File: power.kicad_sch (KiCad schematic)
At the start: 28 parts, among them J3 Conn_01x02, Q2 AO3401A, SW8 SW_Slide_DPDT, U3 TP4056-42-ESOP8, U4 INA219AxDCN, U7 TPS62160DGK

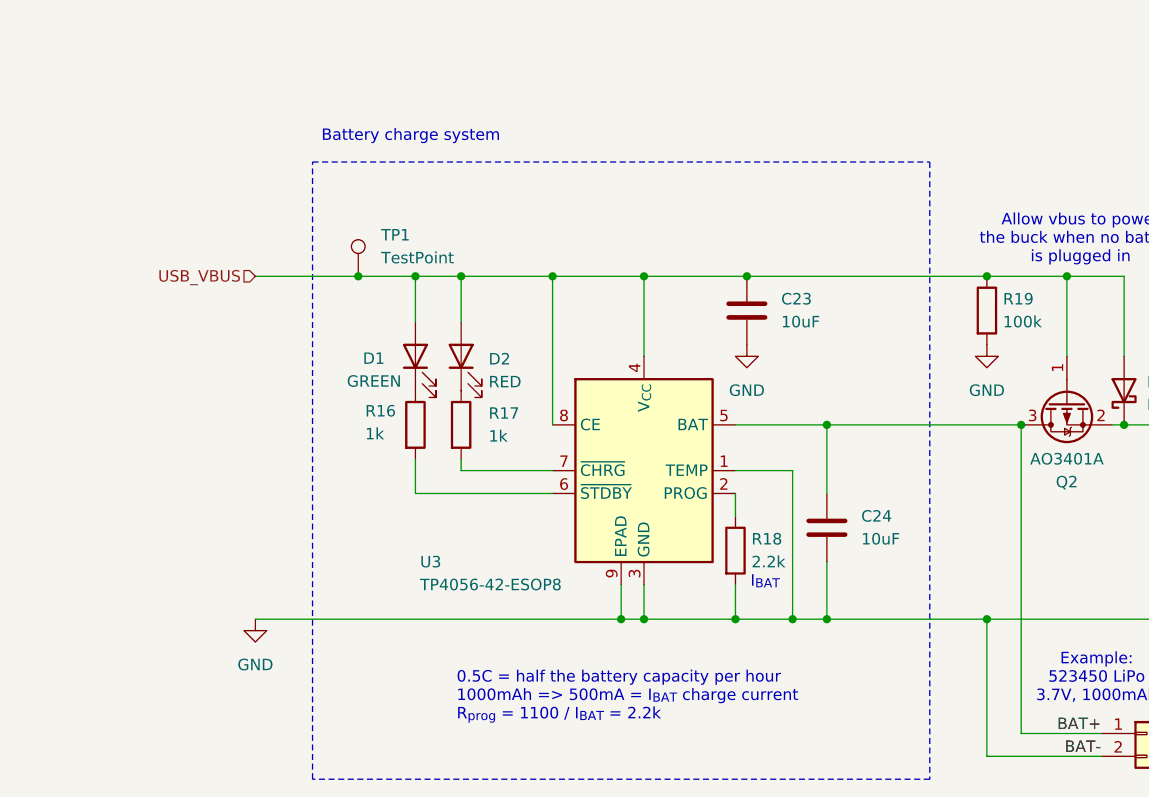
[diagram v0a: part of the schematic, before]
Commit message: add fiducials and mounting holes
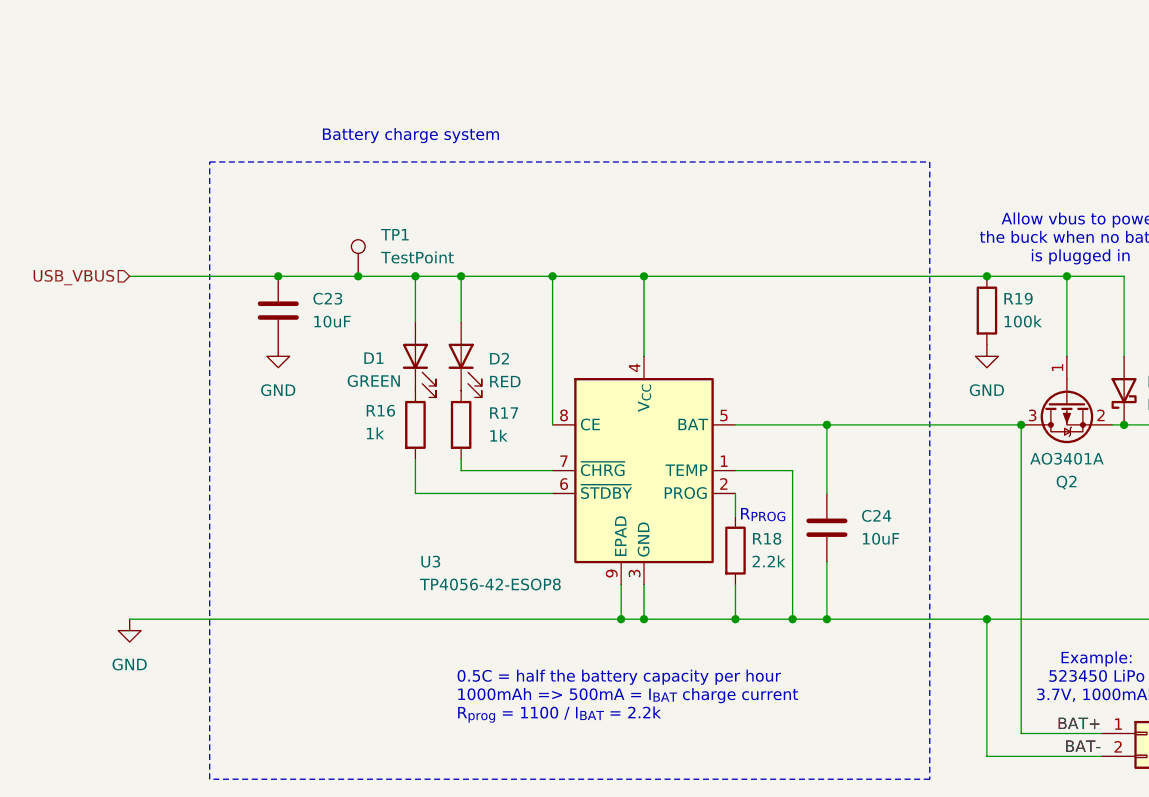
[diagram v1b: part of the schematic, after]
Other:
- note added: "R_{PROG}"
- note removed: "I_{BAT}"
- moved on the sheet: C23
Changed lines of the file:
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@@
 	)
 	(rectangle
-		(start 53.34 60.96)
+		(start 41.91 60.96)
 		(end 121.92 129.54)
 		(stroke
@@
 		)
 	)
-	(text "I_{BAT}"
+	(text "R_{PROG}"
 		(exclude_from_sim no)
-		(at 103.632 107.696 0)
+		(at 103.378 100.33 0)
 		(effects
 			(font
@@
 	)
 	(junction
-		(at 243.84 111.76)
+		(at 49.53 73.66)
 		(diameter 0)
 		(color 0 0 0 0)
 	)
 	(junction
-		(at 218.44 90.17)
+		(at 243.84 111.76)
 		(diameter 0)
 		(color 0 0 0 0)
 	)
 	(junction
-		(at 101.6 73.66)
+		(at 218.44 90.17)
 		(diameter 0)
 		(color 0 0 0 0)
@@
 	(wire
 		(pts
+			(xy 80.01 73.66) (xy 90.17 73.66)
+		)
+		(stroke
+			(width 0)
+			(type default)
+		)
+	)
+	(wire
+		(pts
 			(xy 226.06 57.15) (xy 246.38 57.15)
 		)
@@
 	(wire
 		(pts
-			(xy 46.99 111.76) (xy 87.63 111.76)
+			(xy 33.02 111.76) (xy 87.63 111.76)
 		)
 		(stroke
@@
 	(wire
 		(pts
-			(xy 46.99 73.66) (xy 58.42 73.66)
+			(xy 33.02 73.66) (xy 49.53 73.66)
 		)
 		(stroke
@@
 	(wire
 		(pts
-			(xy 90.17 73.66) (xy 101.6 73.66)
+			(xy 49.53 73.66) (xy 58.42 73.66)
 		)
 		(stroke
@@
 	(wire
 		(pts
-			(xy 80.01 73.66) (xy 90.17 73.66)
+			(xy 69.85 73.66) (xy 80.01 73.66)
 		)
 		(stroke
@@
 	(wire
 		(pts
-			(xy 101.6 73.66) (xy 128.27 73.66)
+			(xy 171.45 90.17) (xy 179.07 90.17)
 		)
 		(stroke
@@
 	(wire
 		(pts
-			(xy 171.45 90.17) (xy 179.07 90.17)
+			(xy 100.33 111.76) (xy 106.68 111.76)
 		)
 		(stroke
@@
 	(wire
 		(pts
-			(xy 100.33 111.76) (xy 106.68 111.76)
+			(xy 110.49 90.17) (xy 132.08 90.17)
 		)
 		(stroke
@@
 	(wire
 		(pts
-			(xy 110.49 90.17) (xy 132.08 90.17)
+			(xy 90.17 73.66) (xy 128.27 73.66)
 		)
 		(stroke
@@
 	(wire
 		(pts
-			(xy 69.85 73.66) (xy 80.01 73.66)
-		)
-		(stroke
-			(width 0)
-			(type default)
-		)
-	)
-	(wire
-		(pts
 			(xy 200.66 111.76) (xy 198.12 111.76)
 		)
@@
 	(hierarchical_label "USB_VBUS"
 		(shape input)
-		(at 46.99 73.66 180)
+		(at 33.02 73.66 180)
 		(effects
 			(font
@@
 	(symbol
 		(lib_id "power:GND")
-		(at 101.6 81.28 0)
+		(at 49.53 81.28 0)
 		(unit 1)
 		(exclude_from_sim no)
@@
 		(fields_autoplaced yes)
 		(property "Reference" "#PWR024"
-			(at 101.6 87.63 0)
+			(at 49.53 87.63 0)
 			(effects
 				(font
@@
 		)
 		(property "Value" "GND"
-			(at 101.6 86.36 0)
+			(at 49.53 86.36 0)
 			(effects
 				(font
@@
 		)
 		(property "Footprint" ""
-			(at 101.6 81.28 0)
+			(at 49.53 81.28 0)
 			(effects
 				(font
@@
 		)
 		(property "Datasheet" ""
-			(at 101.6 81.28 0)
+			(at 49.53 81.28 0)
 			(effects
 				(font
@@
 		)
 		(property "Description" "Power symbol creates a global label with name \"GND\" , ground"
-			(at 101.6 81.28 0)
+			(at 49.53 81.28 0)
 			(effects
 				(font
@@
 	(symbol
 		(lib_id "power:GND")
-		(at 46.99 111.76 0)
+		(at 33.02 111.76 0)
 		(unit 1)
 		(exclude_from_sim no)
@@
 		(fields_autoplaced yes)
 		(property "Reference" "#PWR023"
-			(at 46.99 118.11 0)
+			(at 33.02 118.11 0)
 			(effects
 				(font
@@
 		)
 		(property "Value" "GND"
-			(at 46.99 116.84 0)
+			(at 33.02 116.84 0)
 			(effects
 				(font
@@
 		)
 		(property "Footprint" ""
-			(at 46.99 111.76 0)
+			(at 33.02 111.76 0)
 			(effects
 				(font
@@
 		)
 		(property "Datasheet" ""
-			(at 46.99 111.76 0)
+			(at 33.02 111.76 0)
 			(effects
 				(font
@@
 		)
 		(property "Description" "Power symbol creates a global label with name \"GND\" , ground"
-			(at 46.99 111.76 0)
+			(at 33.02 111.76 0)
 			(effects
 				(font
@@
 	(symbol
 		(lib_id "Device:C")
-		(at 101.6 77.47 0)
+		(at 49.53 77.47 0)
 		(unit 1)
 		(exclude_from_sim no)
@@
 		(fields_autoplaced yes)
 		(property "Reference" "C23"
-			(at 105.41 76.1999 0)
+			(at 53.34 76.1999 0)
 			(effects
 				(font
@@
 		)
 		(property "Value" "10uF"
-			(at 105.41 78.7399 0)
+			(at 53.34 78.7399 0)
 			(effects
 				(font
@@
 		)
 		(property "Footprint" "Capacitor_SMD:C_0805_2012Metric"
-			(at 102.5652 81.28 0)
+			(at 50.4952 81.28 0)
 			(effects
 				(font
@@
 		)
 		(property "Datasheet" "~"
-			(at 101.6 77.47 0)
+			(at 49.53 77.47 0)
 			(effects
 				(font
@@
 		)
 		(property "Description" "Unpolarized capacitor"
-			(at 101.6 77.47 0)
+			(at 49.53 77.47 0)
 			(effects
 				(font
@@
 		)
 		(property "LCSC" ""
-			(at 101.6 77.47 0)
+			(at 49.53 77.47 0)
 			(effects
 				(font
@@
 		)
 		(property "Manufacturer" ""
-			(at 101.6 77.47 0)
+			(at 49.53 77.47 0)
 			(effects
 				(font
@@
 		)
 		(property "Manufacturer Part Number" ""
-			(at 101.6 77.47 0)
+			(at 49.53 77.47 0)
 			(effects
 				(font

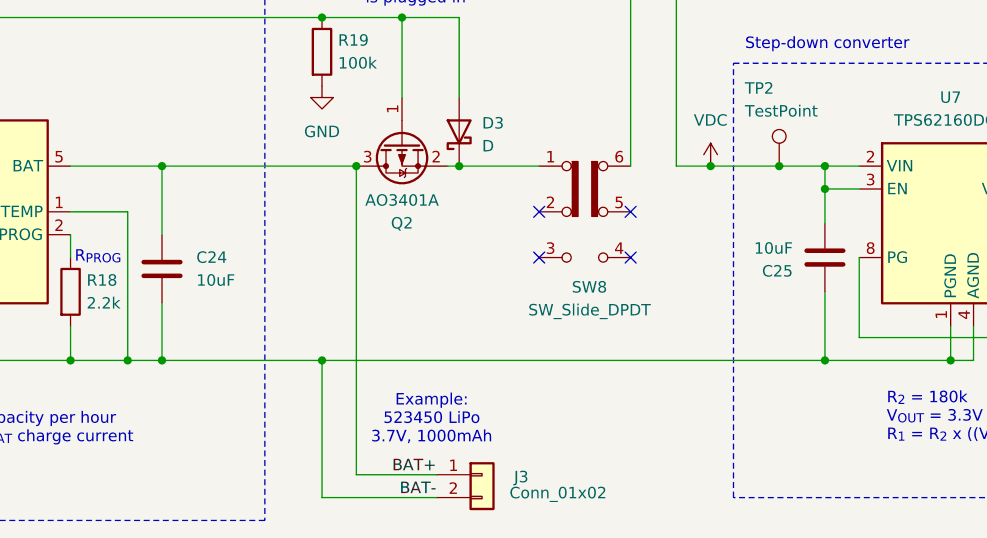
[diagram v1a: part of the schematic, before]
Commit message: battery polarity and position
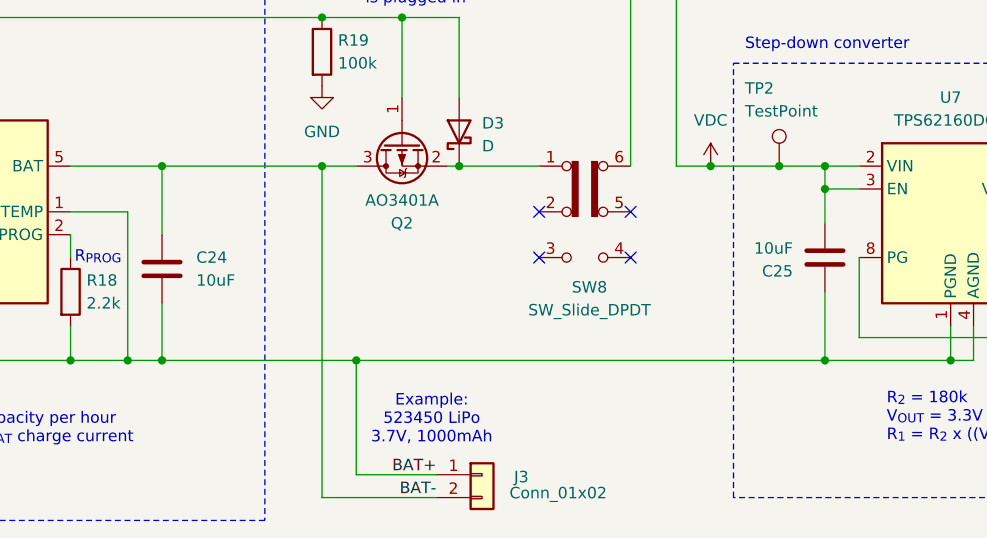
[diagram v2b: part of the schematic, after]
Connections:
- net GND: now also J3.1 (Pin_1); no longer J3.2 (Pin_2)
- net BAT+ renamed BAT-
- net BAT-: now also J3.2 (Pin_2); no longer J3.1 (Pin_1)

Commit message: fix on/off switch routing
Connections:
- net at D3.1 (K), Q2.2 (S): now also SW8.4 (A); no longer SW8.1 (A)
- net at SW8.5 (B): now also R35.1, U4.1 (IN+)
- now unconnected: SW8.6 (C)
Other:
- moved on the sheet: SW8
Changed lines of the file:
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@@
+	)
+	(junction
+		(at 143.51 90.17)
+		(diameter 0)
+		(color 0 0 0 0)
 	)
 	(junction
@@
 	)
 	(junction
-		(at 143.51 90.17)
-		(diameter 0)
-		(color 0 0 0 0)
-	)
-	(junction
 		(at 64.77 73.66)
 		(diameter 0)
@@
 	)
 	(junction
+		(at 128.27 73.66)
+		(diameter 0)
+		(color 0 0 0 0)
+	)
+	(junction
+		(at 198.12 111.76)
+		(diameter 0)
+		(color 0 0 0 0)
+	)
+	(junction
+		(at 214.63 34.29)
+		(diameter 0)
+		(color 0 0 0 0)
+	)
+	(junction
+		(at 184.15 111.76)
+		(diameter 0)
+		(color 0 0 0 0)
+	)
+	(junction
+		(at 106.68 111.76)
+		(diameter 0)
+		(color 0 0 0 0)
+	)
+	(junction
+		(at 90.17 111.76)
+		(diameter 0)
+		(color 0 0 0 0)
+	)
+	(junction
 		(at 193.04 40.64)
 		(diameter 0)
@@
 	)
 	(junction
-		(at 128.27 73.66)
-		(diameter 0)
-		(color 0 0 0 0)
-	)
-	(junction
-		(at 198.12 111.76)
-		(diameter 0)
-		(color 0 0 0 0)
-	)
-	(junction
-		(at 214.63 34.29)
-		(diameter 0)
-		(color 0 0 0 0)
-	)
-	(junction
-		(at 184.15 111.76)
-		(diameter 0)
-		(color 0 0 0 0)
-	)
-	(junction
-		(at 106.68 111.76)
-		(diameter 0)
-		(color 0 0 0 0)
-	)
-	(junction
-		(at 90.17 111.76)
-		(diameter 0)
-		(color 0 0 0 0)
-	)
-	(junction
 		(at 137.16 73.66)
 		(diameter 0)
@@
 	)
 	(no_connect
-		(at 162.56 95.25)
+		(at 154.94 104.14)
 	)
 	(no_connect
-		(at 162.56 100.33)
+		(at 165.1 93.98)
 	)
 	(no_connect
-		(at 152.4 95.25)
+		(at 160.02 104.14)
 	)
 	(no_connect
-		(at 152.4 100.33)
+		(at 165.1 104.14)
 	)
 	(wire
@@
 	(wire
 		(pts
+			(xy 154.94 90.17) (xy 154.94 93.98)
+		)
+		(stroke
+			(width 0)
+			(type default)
+		)
+	)
+	(wire
+		(pts
 			(xy 226.06 57.15) (xy 246.38 57.15)
 		)
@@
 	(wire
 		(pts
-			(xy 162.56 40.64) (xy 162.56 90.17)
-		)
-		(stroke
-			(width 0)
-			(type default)
-		)
-	)
-	(wire
-		(pts
 			(xy 193.04 48.26) (xy 204.47 48.26)
 		)
@@
 	(wire
 		(pts
+			(xy 160.02 40.64) (xy 193.04 40.64)
+		)
+		(stroke
+			(width 0)
+			(type default)
+		)
+	)
+	(wire
+		(pts
 			(xy 184.15 111.76) (xy 198.12 111.76)
 		)
@@
 	(wire
 		(pts
+			(xy 160.02 93.98) (xy 160.02 40.64)
+		)
+		(stroke
+			(width 0)
+			(type default)
+		)
+	)
+	(wire
+		(pts
 			(xy 243.84 90.17) (xy 243.84 96.52)
 		)
@@
 	(wire
 		(pts
-			(xy 193.04 40.64) (xy 162.56 40.64)
-		)
-		(stroke
-			(width 0)
-			(type default)
-		)
-	)
-	(wire
-		(pts
-			(xy 143.51 90.17) (xy 152.4 90.17)
+			(xy 143.51 90.17) (xy 154.94 90.17)
 		)
 		(stroke
@@
 	(symbol
 		(lib_id "Switch:SW_Slide_DPDT")
-		(at 157.48 95.25 0)
+		(at 160.02 99.06 270)
+		(mirror x)
 		(unit 1)
 		(body_style 1)
@@
 		(dnp no)
 		(property "Reference" "SW8"
-			(at 157.988 103.632 0)
+			(at 160.274 109.474 90)
 			(show_name no)
 			(do_not_autoplace no)
@@
 		)
 		(property "Value" "SW_Slide_DPDT"
-			(at 157.988 106.172 0)
+			(at 160.274 106.934 90)
 			(show_name no)
 			(do_not_autoplace no)
@@
 		)
 		(property "Footprint" "Button_Switch_SMD:SW_DPDT_CK_JS202011JCQN"
-			(at 171.45 90.17 0)
+			(at 165.1 85.09 0)
 			(hide yes)
 			(show_name no)
@@
 		)
 		(property "Datasheet" ""
-			(at 157.48 95.25 0)
+			(at 160.02 99.06 0)
 			(hide yes)
 			(show_name no)
@@
 		)
 		(property "Description" "Slide Switch, dual pole double throw"
-			(at 157.48 95.25 0)
+			(at 160.02 99.06 0)
 			(hide yes)
 			(show_name no)
@@
 		)
 		(property "LCSC" "C221665"
-			(at 157.48 95.25 0)
+			(at 160.02 99.06 0)
 			(hide yes)
 			(show_name no)
@@
 		)
 		(property "Manufacturer" "C&K"
-			(at 157.48 95.25 0)
+			(at 160.02 99.06 0)
 			(hide yes)
 			(show_name no)
@@
 		)
 		(property "Manufacturer Part Number" "JS202011JCQN"
-			(at 157.48 95.25 0)
-			(hide yes)
-			(show_name no)
+			(at 160.02 99.06 0)
+			(hide yes)
+			(show_name no)
